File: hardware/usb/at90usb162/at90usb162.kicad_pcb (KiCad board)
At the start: 2 copper layers, 47.5 x 34.8 mm, 13 parts, among them IC1 AT90USB162-A, J1 USERPORT, P1 USB, P2 RESET, X1 8Mhz

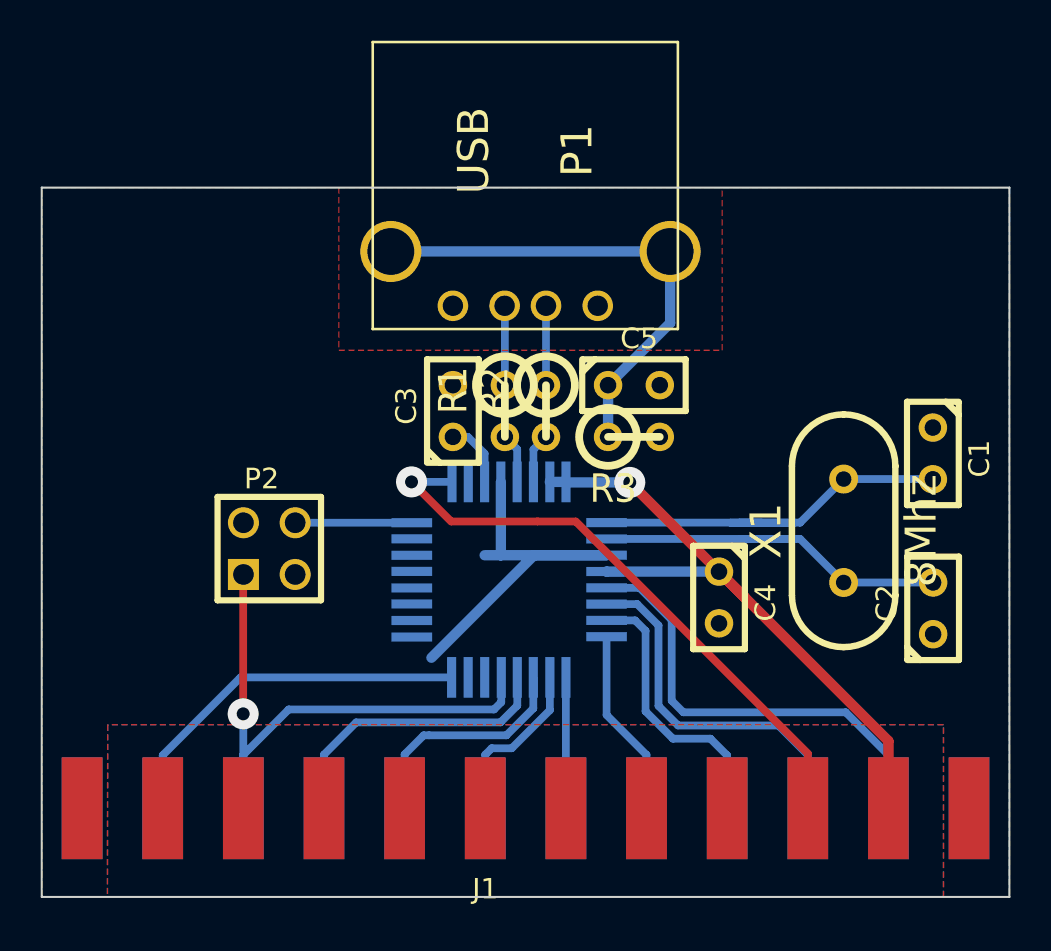
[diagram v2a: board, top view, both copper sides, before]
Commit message: Hardware: Enlarged board to increase stability of usb socket
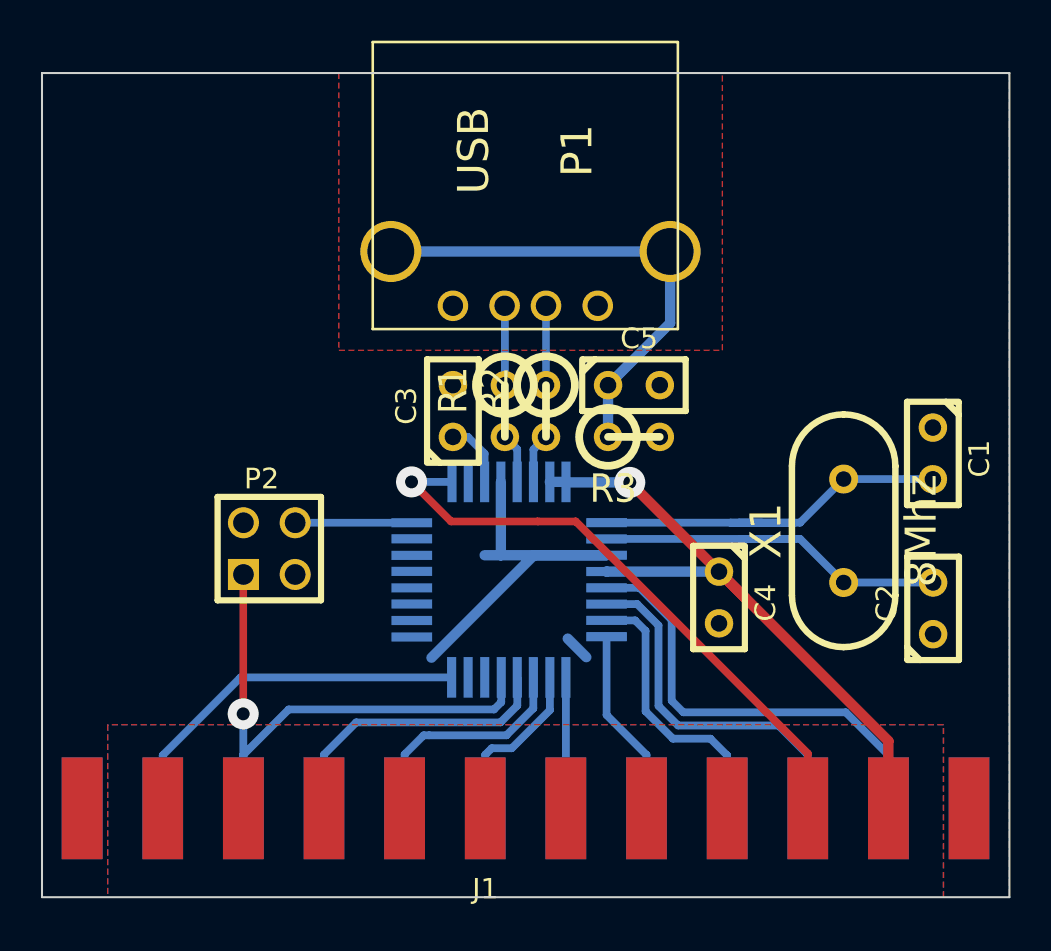
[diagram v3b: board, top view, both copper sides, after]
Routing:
- net GND: track 20.3 -> 21.6 mm
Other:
- board size 47.5 x 34.8 mm -> 47.5 x 40.5 mm
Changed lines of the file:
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@@
     (links 43)
     (no_connects 0)
-    (area 178.563599 114.211099 255.5738 165.6537)
+    (area 178.563599 112.752199 277.367 165.6537)
     (thickness 1.6)
-    (drawings 37)
-    (tracks 109)
+    (drawings 47)
+    (tracks 110)
     (zones 0)
     (modules 13)
@@
     (last_trace_width 0.381)
     (trace_clearance 0.254)
-    (zone_clearance 0.508)
+    (zone_clearance 0.381)
     (zone_45_only no)
     (trace_min 0.254)
@@
     )
   )
+  (dimension 40.4749 (width 0.3) (layer Dwgs.User)
+    (gr_text "40,475 mm" (at 270.717 136.29005 90) (layer Dwgs.User)
+      (effects (font (size 1.5 1.5) (thickness 0.3)))
+    )
+    (feature1 (pts (xy 234.1245 116.0526) (xy 272.067 116.0526)))
+    (feature2 (pts (xy 234.1245 156.5275) (xy 272.067 156.5275)))
+    (crossbar (pts (xy 269.367 156.5275) (xy 269.367 116.0526)))
+    (arrow1a (pts (xy 269.367 116.0526) (xy 269.95342 117.179103)))
+    (arrow1b (pts (xy 269.367 116.0526) (xy 268.78058 117.179103)))
+    (arrow2a (pts (xy 269.367 156.5275) (xy 269.95342 155.400997)))
+    (arrow2b (pts (xy 269.367 156.5275) (xy 268.78058 155.400997)))
+  )
+  (gr_line (start 234.1245 156.5275) (end 186.6138 156.5275) (angle 90) (layer Edge.Cuts) (width 0.1))
+  (gr_line (start 234.1245 116.0526) (end 234.1245 156.5275) (angle 90) (layer Edge.Cuts) (width 0.1))
+  (gr_line (start 186.6138 116.0526) (end 234.1245 116.0526) (angle 90) (layer Edge.Cuts) (width 0.1))
+  (gr_line (start 186.6138 156.5275) (end 186.6138 116.0526) (angle 90) (layer Edge.Cuts) (width 0.1))
+  (gr_line (start 230.886 156.5148) (end 230.886 148.0693) (angle 90) (layer Dwgs.User) (width 0.2))
+  (gr_line (start 189.8396 148.0058) (end 189.8269 148.0058) (angle 90) (layer Dwgs.User) (width 0.2))
+  (gr_line (start 189.8396 156.5021) (end 189.8396 148.0058) (angle 90) (layer Dwgs.User) (width 0.2))
+  (gr_line (start 244.0305 156.5148) (end 244.0305 156.5275) (angle 90) (layer Dwgs.User) (width 0.2))
+  (gr_line (start 186.6011 156.5148) (end 244.0305 156.5148) (angle 90) (layer Dwgs.User) (width 0.2))
+  (gr_line (start 234.1245 116.0399) (end 234.1372 116.0399) (angle 90) (layer Dwgs.User) (width 0.2))
+  (gr_line (start 234.1245 121.8692) (end 234.1245 116.0399) (angle 90) (layer Dwgs.User) (width 0.2))
+  (gr_line (start 237.1725 116.0526) (end 237.1725 115.9764) (angle 90) (layer Dwgs.User) (width 0.2))
+  (gr_line (start 186.5757 116.0526) (end 237.1725 116.0526) (angle 90) (layer Dwgs.User) (width 0.2))
+  (gr_line (start 186.6011 121.7803) (end 186.6011 114.0968) (angle 90) (layer Dwgs.User) (width 0.2))
+  (gr_line (start 220.0148 112.8903) (end 219.837 112.8903) (angle 90) (layer Dwgs.User) (width 0.2))
+  (gr_line (start 220.0148 129.6543) (end 220.0148 112.8903) (angle 90) (layer Dwgs.User) (width 0.2))
+  (gr_line (start 201.1934 112.8522) (end 201.2188 112.8522) (angle 90) (layer Dwgs.User) (width 0.2))
+  (gr_line (start 201.1934 124.8664) (end 201.1934 112.8522) (angle 90) (layer Dwgs.User) (width 0.2))
   (gr_line (start 222.1738 138.5316) (end 189.992 138.5316) (angle 90) (layer Dwgs.User) (width 0.2))
   (gr_line (start 196.4944 147.5105) (end 196.4944 141.9098) (angle 90) (layer Dwgs.User) (width 0.2))
   (gr_line (start 187.7949 132.6515) (end 187.7949 132.6261) (angle 90) (layer Dwgs.User) (width 0.2))
   (gr_line (start 224.0915 132.6515) (end 187.7949 132.6515) (angle 90) (layer Dwgs.User) (width 0.2))
-  (dimension 34.8361 (width 0.3) (layer Dwgs.User)
-    (gr_text "34,836 mm" (at 248.9238 139.09675 90) (layer Dwgs.User)
-      (effects (font (size 1.5 1.5) (thickness 0.3)))
-    )
-    (feature1 (pts (xy 234.1245 121.6787) (xy 250.2738 121.6787)))
-    (feature2 (pts (xy 234.1245 156.5148) (xy 250.2738 156.5148)))
-    (crossbar (pts (xy 247.5738 156.5148) (xy 247.5738 121.6787)))
-    (arrow1a (pts (xy 247.5738 121.6787) (xy 248.16022 122.805203)))
-    (arrow1b (pts (xy 247.5738 121.6787) (xy 246.98738 122.805203)))
-    (arrow2a (pts (xy 247.5738 156.5148) (xy 248.16022 155.388297)))
-    (arrow2b (pts (xy 247.5738 156.5148) (xy 246.98738 155.388297)))
-  )
   (dimension 47.5234 (width 0.3) (layer Dwgs.User)
     (gr_text "47,523 mm" (at 210.3628 164.303699) (layer Dwgs.User)
@@
   (gr_line (start 199.4535 129.667) (end 220.5863 129.667) (angle 90) (layer Dwgs.User) (width 0.2))
   (gr_line (start 201.1553 131.3688) (end 201.1299 131.3688) (angle 90) (layer Dwgs.User) (width 0.2))
-  (gr_line (start 234.1245 156.5148) (end 186.6011 156.5148) (angle 90) (layer Edge.Cuts) (width 0.1))
-  (gr_line (start 234.1245 121.6787) (end 234.1245 156.5148) (angle 90) (layer Edge.Cuts) (width 0.1))
-  (gr_line (start 186.6011 121.6787) (end 234.1245 121.6787) (angle 90) (layer Edge.Cuts) (width 0.1))
-  (gr_line (start 186.6011 156.5148) (end 186.6011 121.6787) (angle 90) (layer Edge.Cuts) (width 0.1))
   (gr_line (start 234.1245 154.6606) (end 234.1245 121.3358) (angle 90) (layer Dwgs.User) (width 0.2))
   (gr_line (start 244.7544 121.6787) (end 244.7544 121.6914) (angle 90) (layer Dwgs.User) (width 0.2))
   (gr_line (start 210.2612 121.6787) (end 244.7544 121.6787) (angle 90) (layer Dwgs.User) (width 0.2))
   (gr_line (start 210.2358 121.6787) (end 178.6636 121.6787) (angle 90) (layer Dwgs.User) (width 0.2))
-  (target plus (at 234.1245 156.5148) (size 0.005) (width 0.1) (layer Edge.Cuts))
-  (target plus (at 234.1245 154.6606) (size 0.005) (width 0.1) (layer Edge.Cuts))
-  (target plus (at 186.6011 156.5148) (size 0.005) (width 0.1) (layer Edge.Cuts))
-  (target plus (at 186.6011 154.6733) (size 0.005) (width 0.1) (layer Edge.Cuts))
   (gr_line (start 228.4603 142.3416) (end 228.4603 125.8951) (angle 90) (layer Dwgs.User) (width 0.2))
   (gr_line (start 213.3981 138.5316) (end 230.6066 138.5316) (angle 90) (layer Dwgs.User) (width 0.2))
@@
   (segment (start 217.5383 142.9131) (end 217.5383 146.875498) (width 0.381) (layer B.Cu) (net 15))
   (segment (start 215.95842 141.33322) (end 217.5383 142.9131) (width 0.381) (layer B.Cu) (net 15))
+  (segment (start 213.3473 144.7419) (end 212.4329 143.8275) (width 0.508) (layer B.Cu) (net 16))
   (segment (start 214.34044 139.73302) (end 210.77428 139.73302) (width 0.508) (layer B.Cu) (net 16))
   (segment (start 210.77428 139.73302) (end 205.74 144.7673) (width 0.508) (layer B.Cu) (net 16))
@@
   (segment (start 228.1816 148.8574) (end 221.15145 141.82725) (width 0.508) (layer F.Cu) (net 22))
   (segment (start 221.15145 141.82725) (end 219.8624 140.5382) (width 0.508) (layer F.Cu) (net 22))
-  (zone (net 16) (net_name GND) (layer B.Cu) (hatch edge 0.508)
-    (connect_pads yes (clearance 0.508))
-    (min_thickness 0.254)
-    (fill (arc_segments 32) (thermal_gap 0.508) (thermal_bridge_width 0.508) (smoothing fillet))
+  (zone (net 16) (net_name GND) (layer F.Cu) (hatch edge 0.508)
+    (connect_pads thru_hole_only (clearance 0.381))
+    (min_thickness 0.0254)
+    (fill (arc_segments 32) (thermal_gap 0.508) (thermal_bridge_width 0.508) (smoothing chamfer))
     (polygon
       (pts
-        (xy 234.1245 121.6914) (xy 234.1118 156.5021) (xy 230.886 156.5021) (xy 230.886 148.0566) (xy 189.8396 148.0566)
-        (xy 189.8269 156.5148) (xy 186.6011 156.5148) (xy 186.6011 121.6787)
+        (xy 234.1245 156.5275) (xy 230.886 156.5275) (xy 230.886 148.0566) (xy 189.8396 148.0566) (xy 189.8396 156.5275)
+        (xy 186.6138 156.5275) (xy 186.6138 116.0526) (xy 201.1934 116.0526) (xy 201.1934 129.667) (xy 220.0275 129.667)
+        (xy 220.0275 116.0526) (xy 234.1245 116.0653)
       )
     )
   )
-  (zone (net 16) (net_name GND) (layer F.Cu) (hatch edge 0.508)
-    (connect_pads yes (clearance 0.508))
-    (min_thickness 0.254)
-    (fill (arc_segments 32) (thermal_gap 0.508) (thermal_bridge_width 0.508) (smoothing fillet))
+  (zone (net 16) (net_name GND) (layer B.Cu) (hatch edge 0.508)
+    (connect_pads thru_hole_only (clearance 0.381))
+    (min_thickness 0.0254)
+    (fill (arc_segments 32) (thermal_gap 0.508) (thermal_bridge_width 0.508) (smoothing chamfer))
     (polygon
       (pts
-        (xy 234.1245 156.5148) (xy 230.886 156.5148) (xy 230.886 148.0566) (xy 189.8396 148.0566) (xy 189.8269 156.5148)
-        (xy 186.6011 156.5148) (xy 186.6011 121.6787) (xy 201.1934 121.6787) (xy 201.1934 129.667) (xy 220.0148 129.667)
-        (xy 220.0148 121.6787) (xy 234.1245 121.6787)
+        (xy 186.6138 156.5275) (xy 186.6138 116.0526) (xy 234.1245 116.0653) (xy 234.1245 156.5275) (xy 230.886 156.5275)
+        (xy 230.886 148.0566) (xy 189.8396 148.0566) (xy 189.8396 156.5275)
       )
     )

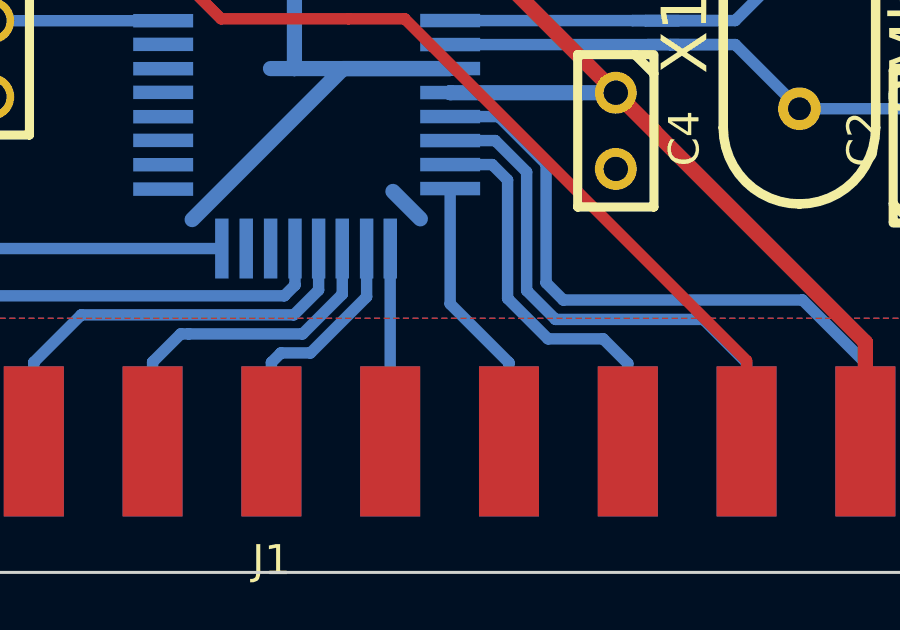
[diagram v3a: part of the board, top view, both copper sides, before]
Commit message: Hardware: Removed copper island, improved routing
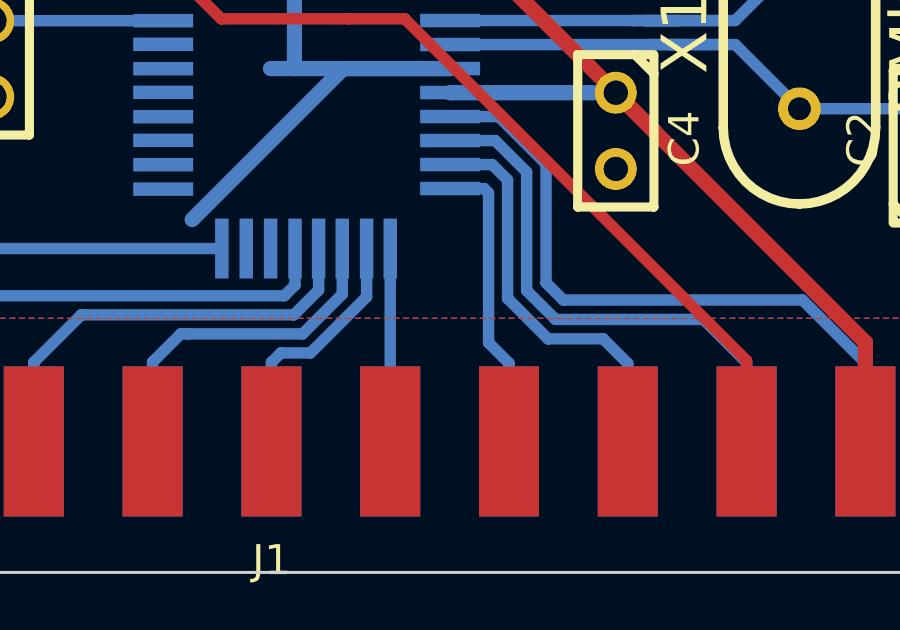
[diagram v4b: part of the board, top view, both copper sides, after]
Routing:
- net GND: track 21.6 -> 20.3 mm
- net /D2: track 9.24 -> 9.91 mm
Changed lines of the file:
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@@
     (thickness 1.6)
     (drawings 47)
-    (tracks 110)
+    (tracks 111)
     (zones 0)
     (modules 13)
@@
   (segment (start 216.2556 147.3962) (end 217.6018 148.7424) (width 0.381) (layer B.Cu) (net 6))
   (segment (start 217.6018 148.7424) (end 219.4433 148.7424) (width 0.381) (layer B.Cu) (net 6))
-  (segment (start 214.34044 143.73352) (end 214.34044 147.57654) (width 0.381) (layer B.Cu) (net 7))
-  (segment (start 216.3016 149.5377) (end 216.3016 152.1611) (width 0.381) (layer B.Cu) (net 7))
-  (segment (start 214.34044 147.57654) (end 216.3016 149.5377) (width 0.381) (layer B.Cu) (net 7))
+  (segment (start 216.3016 152.1611) (end 216.3016 149.5504) (width 0.381) (layer B.Cu) (net 7) (status 400000))
+  (segment (start 215.47582 143.73352) (end 214.34044 143.73352) (width 0.381) (layer B.Cu) (net 7) (status 800000))
+  (segment (start 215.620598 143.878298) (end 215.47582 143.73352) (width 0.381) (layer B.Cu) (net 7))
+  (segment (start 215.620598 148.869398) (end 215.620598 143.878298) (width 0.381) (layer B.Cu) (net 7))
+  (segment (start 216.3016 149.5504) (end 215.620598 148.869398) (width 0.381) (layer B.Cu) (net 7))
   (segment (start 212.3416 152.1611) (end 212.3416 145.7349) (width 0.381) (layer B.Cu) (net 8))
   (segment (start 212.3416 145.7349) (end 212.344 145.7325) (width 0.381) (layer B.Cu) (net 8))
@@
   (segment (start 217.5383 142.9131) (end 217.5383 146.875498) (width 0.381) (layer B.Cu) (net 15))
   (segment (start 215.95842 141.33322) (end 217.5383 142.9131) (width 0.381) (layer B.Cu) (net 15))
-  (segment (start 213.3473 144.7419) (end 212.4329 143.8275) (width 0.508) (layer B.Cu) (net 16))
   (segment (start 214.34044 139.73302) (end 210.77428 139.73302) (width 0.508) (layer B.Cu) (net 16))
   (segment (start 210.77428 139.73302) (end 205.74 144.7673) (width 0.508) (layer B.Cu) (net 16))
